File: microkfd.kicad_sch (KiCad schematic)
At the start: 47 parts, among them J1 USB_B_Micro, J2 AudioJack3, J3 OLED, Q1 2N7002, Q2 2N7002, SW1 RST, SW2 DOWN, SW3 ENT, SW4 UP, U1 SP3003-02, U2 ATmega32U4RC-A, Y1 16MHz

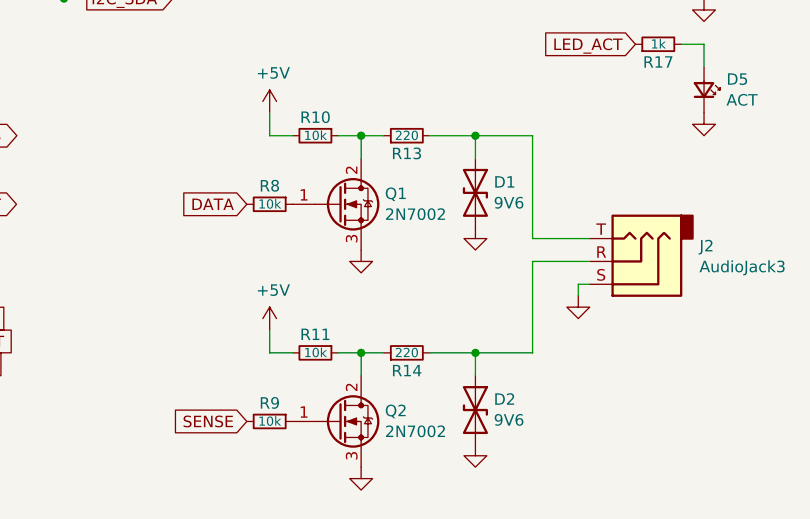
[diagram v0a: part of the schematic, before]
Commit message: finalized rev B
switched MOSFETs due to parts availability, regenerated gerbers
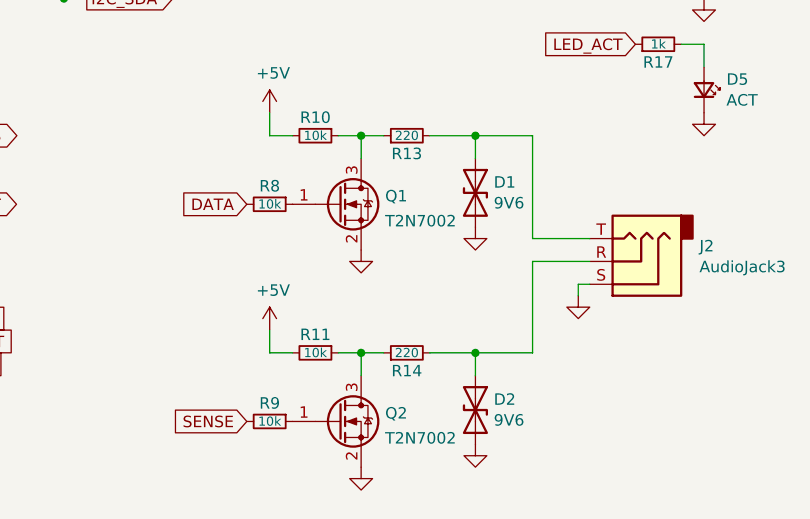
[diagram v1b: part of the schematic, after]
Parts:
- removed Q1, Q2: 2N7002, Package_TO_SOT_SMD:SOT-23_Handsoldering, symbol Device:Q_NMOS_GDS
- added Q1, Q2: T2N7002, Package_TO_SOT_SMD:SOT-23_Handsoldering, symbol Device:Q_NMOS_GSD
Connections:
- net GND: now also Q1.2 (S), Q2.2 (S)
- net at R8.1: now also Q1.1 (G)
- net at R10.1, R13.1: now also Q1.3 (D)
- net at R9.1: now also Q2.1 (G)
- net at R11.1, R14.1: now also Q2.3 (D)
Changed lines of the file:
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@@
     (pin "1")
-  )
-  (symbol (lib_id "Device:Q_NMOS_GDS") (at 162.56 114.3 0) (unit 1)
-    (in_bom yes) (on_board yes)
-    (property "Reference" "Q1" (id 0) (at 167.7416 113.1316 0)
-      (effects (font (size 1.27 1.27)) (justify left))
-    )
-    (property "Value" "2N7002" (id 1) (at 167.7416 115.443 0)
-      (effects (font (size 1.27 1.27)) (justify left))
-    )
-    (property "Footprint" "Package_TO_SOT_SMD:SOT-23_Handsoldering" (id 2) (at 167.64 111.76 0)
-      (effects (font (size 1.27 1.27)) hide)
-    )
-    (property "Datasheet" "~" (id 3) (at 162.56 114.3 0)
-      (effects (font (size 1.27 1.27)) hide)
-    )
-    (pin "1")
-    (pin "2")
-    (pin "3")
   )
   (symbol (lib_id "Device:R_Small") (at 154.94 114.3 270) (unit 1)
@@
     (pin "1")
   )
-  (symbol (lib_id "Device:Q_NMOS_GDS") (at 162.56 138.43 0) (unit 1)
-    (in_bom yes) (on_board yes)
-    (property "Reference" "Q2" (id 0) (at 167.7416 137.2616 0)
-      (effects (font (size 1.27 1.27)) (justify left))
-    )
-    (property "Value" "2N7002" (id 1) (at 167.7416 139.573 0)
-      (effects (font (size 1.27 1.27)) (justify left))
-    )
-    (property "Footprint" "Package_TO_SOT_SMD:SOT-23_Handsoldering" (id 2) (at 167.64 135.89 0)
-      (effects (font (size 1.27 1.27)) hide)
-    )
-    (property "Datasheet" "~" (id 3) (at 162.56 138.43 0)
-      (effects (font (size 1.27 1.27)) hide)
-    )
-    (pin "1")
-    (pin "2")
-    (pin "3")
-  )
   (symbol (lib_id "Device:R_Small") (at 154.94 138.43 270) (unit 1)
     (in_bom yes) (on_board yes)
@@
     (pin "1")
     (pin "2")
+  )
+  (symbol (lib_id "Device:Q_NMOS_GSD") (at 162.56 114.3 0) (unit 1)
+    (in_bom yes) (on_board yes) (fields_autoplaced)
+    (property "Reference" "Q1" (id 0) (at 167.767 113.3915 0)
+      (effects (font (size 1.27 1.27)) (justify left))
+    )
+    (property "Value" "T2N7002" (id 1) (at 167.767 116.1666 0)
+      (effects (font (size 1.27 1.27)) (justify left))
+    )
+    (property "Footprint" "Package_TO_SOT_SMD:SOT-23_Handsoldering" (id 2) (at 167.64 111.76 0)
+      (effects (font (size 1.27 1.27)) hide)
+    )
+    (property "Datasheet" "~" (id 3) (at 162.56 114.3 0)
+      (effects (font (size 1.27 1.27)) hide)
+    )
+    (pin "1")
+    (pin "2")
+    (pin "3")
   )
   (symbol (lib_id "MCU_Microchip_ATmega:ATmega32U4RC-A") (at 101.6 96.52 0) (unit 1)
@@
     (pin "9")
   )
+  (symbol (lib_id "Device:Q_NMOS_GSD") (at 162.56 138.43 0) (unit 1)
+    (in_bom yes) (on_board yes) (fields_autoplaced)
+    (property "Reference" "Q2" (id 0) (at 167.767 137.5215 0)
+      (effects (font (size 1.27 1.27)) (justify left))
+    )
+    (property "Value" "T2N7002" (id 1) (at 167.767 140.2966 0)
+      (effects (font (size 1.27 1.27)) (justify left))
+    )
+    (property "Footprint" "Package_TO_SOT_SMD:SOT-23_Handsoldering" (id 2) (at 167.64 135.89 0)
+      (effects (font (size 1.27 1.27)) hide)
+    )
+    (property "Datasheet" "~" (id 3) (at 162.56 138.43 0)
+      (effects (font (size 1.27 1.27)) hide)
+    )
+    (pin "1")
+    (pin "2")
+    (pin "3")
+  )
   (sheet_instances
     (path "/" (page "1"))
@@
       (reference "J3") (unit 1) (value "OLED") (footprint "Connector_PinSocket_2.54mm:PinSocket_1x04_P2.54mm_Vertical_SMD_Pin1Left")
     )
-    (path "/00000000-0000-0000-0000-000061af1fd1"
-      (reference "Q1") (unit 1) (value "2N7002") (footprint "Package_TO_SOT_SMD:SOT-23_Handsoldering")
-    )
-    (path "/00000000-0000-0000-0000-000061ba989c"
-      (reference "Q2") (unit 1) (value "2N7002") (footprint "Package_TO_SOT_SMD:SOT-23_Handsoldering")
+    (path "/5f7c53ad-a221-4a7c-aa56-8fe23dde6e72"
+      (reference "Q1") (unit 1) (value "T2N7002") (footprint "Package_TO_SOT_SMD:SOT-23_Handsoldering")
+    )
+    (path "/a8941a1d-02e4-4d2e-8a0e-8e48b9dc4893"
+      (reference "Q2") (unit 1) (value "T2N7002") (footprint "Package_TO_SOT_SMD:SOT-23_Handsoldering")
     )
     (path "/00000000-0000-0000-0000-000061ae9c86"

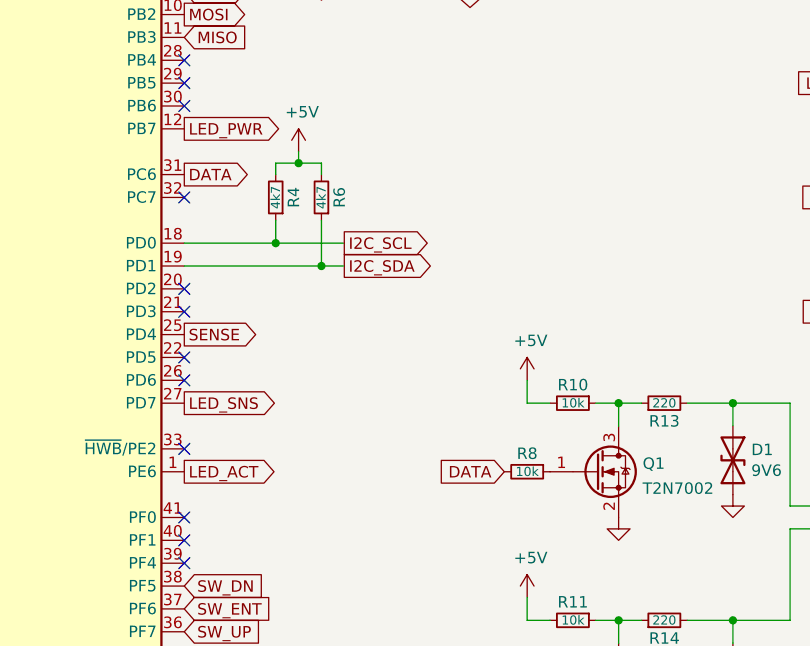
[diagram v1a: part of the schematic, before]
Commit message: revC updates
fixed missing data input line (now runs to PC2 interrupt pin)
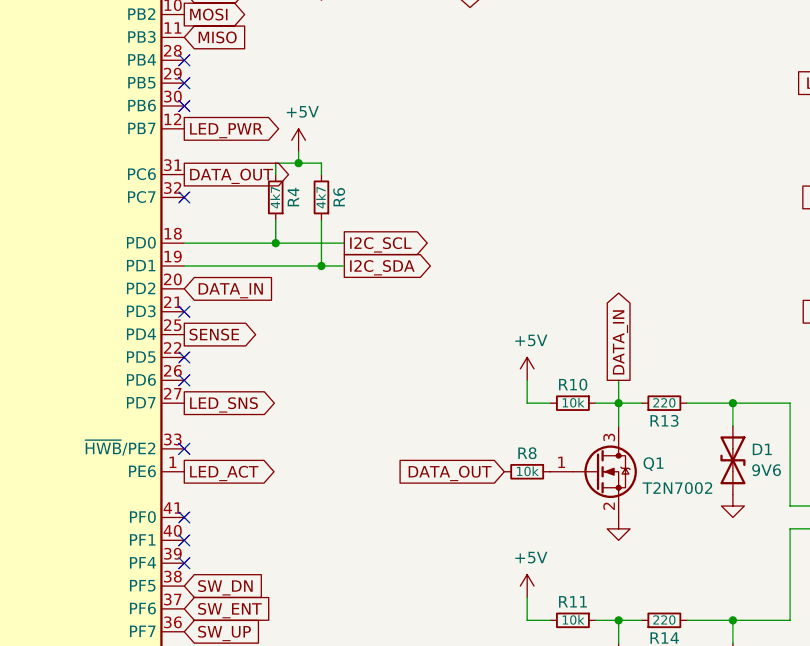
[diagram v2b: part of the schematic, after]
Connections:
- net DATA_IN: now reaches Q1.3 (D), R10.1, R13.1
- net DATA_IN: now also U2.20 (PD2)
- net DATA renamed DATA_OUT
- no-connect marks 15 -> 14
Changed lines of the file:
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@@
   (title_block
     (title "MicroKFD")
-    (date "2021-12-06")
-    (rev "A")
+    (date "2022-01-19")
+    (rev "C")
     (company "W3AXL")
-    (comment 2 "https://github.com/jelimoore/KFDtool")
-    (comment 3 "Based on the KFDShield")
+    (comment 1 "https://github.com/jelimoore/KFDtool")
+    (comment 2 "Based on the KFDShield")
+    (comment 4 "2022-01-19: Fixed missing data input line")
   )
   (junction (at 127 88.9) (diameter 0) (color 0 0 0 0)
@@
   (junction (at 76.2 78.74) (diameter 0) (color 0 0 0 0)
   )
-  (no_connect (at 116.84 93.98))
   (no_connect (at 116.84 96.52))
   (no_connect (at 116.84 58.42))
@@
     (stroke (width 0) (type default) (color 0 0 0 0))
   )
+  (wire (pts (xy 165.1 104.14) (xy 165.1 106.68))
+    (stroke (width 0) (type default) (color 0 0 0 0))
+  )
   (wire (pts (xy 195.58 55.88) (xy 195.58 48.26))
     (stroke (width 0) (type default) (color 0 0 0 0))
@@
     (effects (font (size 1.27 1.27)) (justify left bottom))
   )
-  (global_label "DATA" (shape output) (at 116.84 81.28 0) (fields_autoplaced)
-    (effects (font (size 1.27 1.27)) (justify left))
-    (property "Intersheet References" "${INTERSHEET_REFS}" (id 0) (at 0 0 0)
-      (effects (font (size 1.27 1.27)) hide)
+  (global_label "DATA_IN" (shape input) (at 116.84 93.98 0) (fields_autoplaced)
+    (effects (font (size 1.27 1.27)) (justify left))
+    (property "Intersheet References" "${INTERSHEET_REFS}" (id 0) (at 126.4818 93.9006 0)
+      (effects (font (size 1.27 1.27)) (justify left) hide)
+    )
+  )
+  (global_label "DATA_OUT" (shape output) (at 116.84 81.28 0) (fields_autoplaced)
+    (effects (font (size 1.27 1.27)) (justify left))
+    (property "Intersheet References" "${INTERSHEET_REFS}" (id 0) (at 128.1752 81.2006 0)
+      (effects (font (size 1.27 1.27)) (justify left) hide)
     )
   )
@@
     )
   )
-  (global_label "DATA" (shape input) (at 152.4 114.3 180) (fields_autoplaced)
+  (global_label "DATA_OUT" (shape input) (at 152.4 114.3 180) (fields_autoplaced)
     (effects (font (size 1.27 1.27)) (justify right))
-    (property "Intersheet References" "${INTERSHEET_REFS}" (id 0) (at 0 0 0)
-      (effects (font (size 1.27 1.27)) hide)
+    (property "Intersheet References" "${INTERSHEET_REFS}" (id 0) (at 141.0648 114.2206 0)
+      (effects (font (size 1.27 1.27)) (justify right) hide)
     )
   )
@@
     )
   )
+  (global_label "DATA_IN" (shape output) (at 165.1 104.14 90) (fields_autoplaced)
+    (effects (font (size 1.27 1.27)) (justify left))
+    (property "Intersheet References" "${INTERSHEET_REFS}" (id 0) (at 165.0206 94.4982 90)
+      (effects (font (size 1.27 1.27)) (justify left) hide)
+    )
+  )

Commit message: rev D: fixed pin mappings
changed pin mappings to be closer to original KFDShield, added correct sense and data lines
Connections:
- net SW_DN: now also U2.37 (PF6); no longer U2.38 (PF5)
- net SW_ENT: now also U2.38 (PF5); no longer U2.37 (PF6)
- net SENSE_IN: now reaches Q2.3 (D), R11.1, R14.1
- net SENSE_IN: now also U2.21 (PD3)
- net SENSE renamed SENSE_OUT
- no-connect marks 14 -> 13
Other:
- moved on the sheet: R4, R6

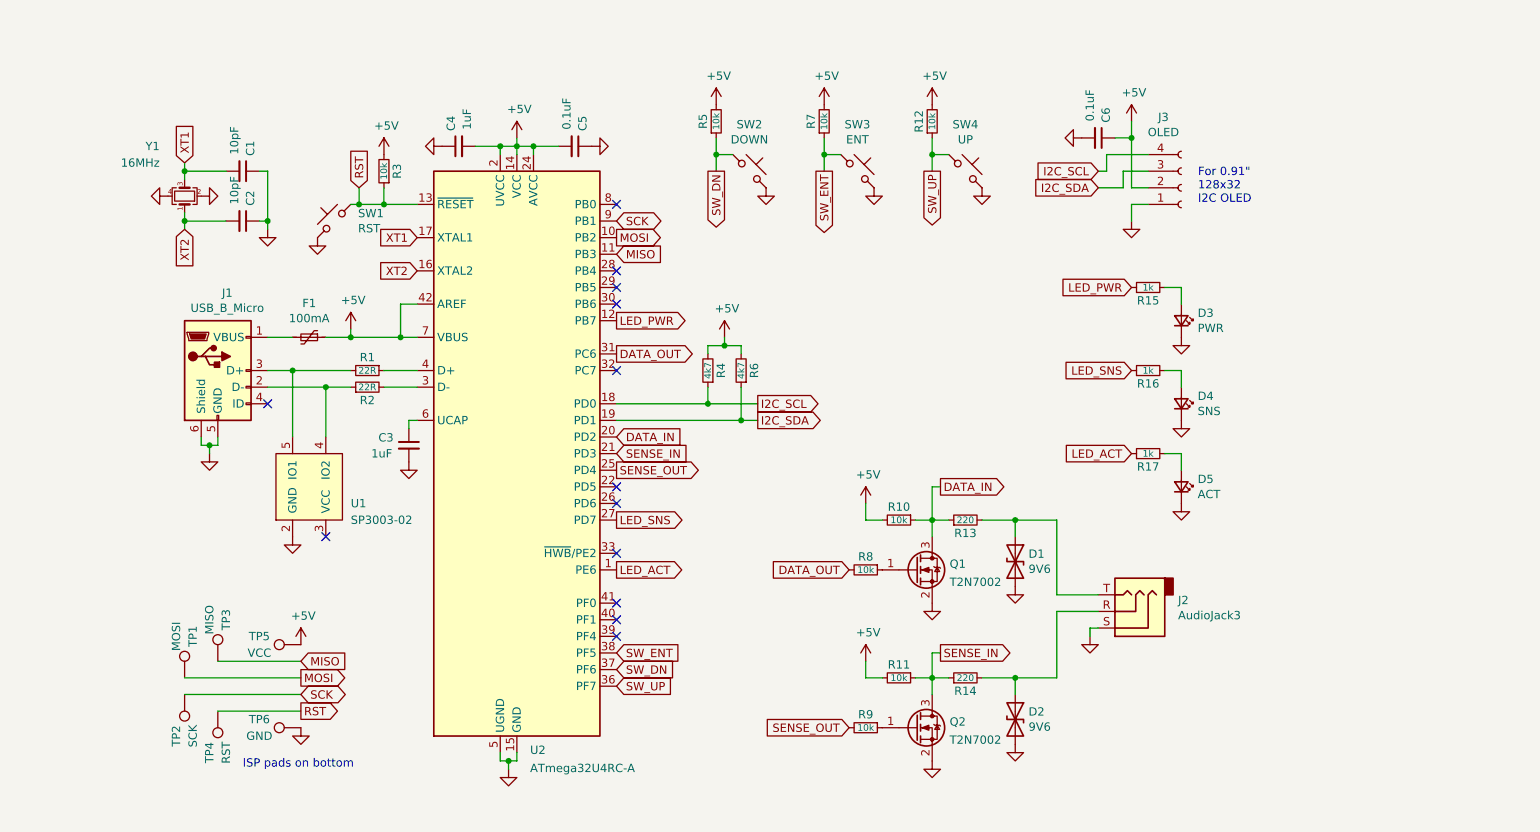
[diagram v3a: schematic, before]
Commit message: revision E - atmega328p redesign
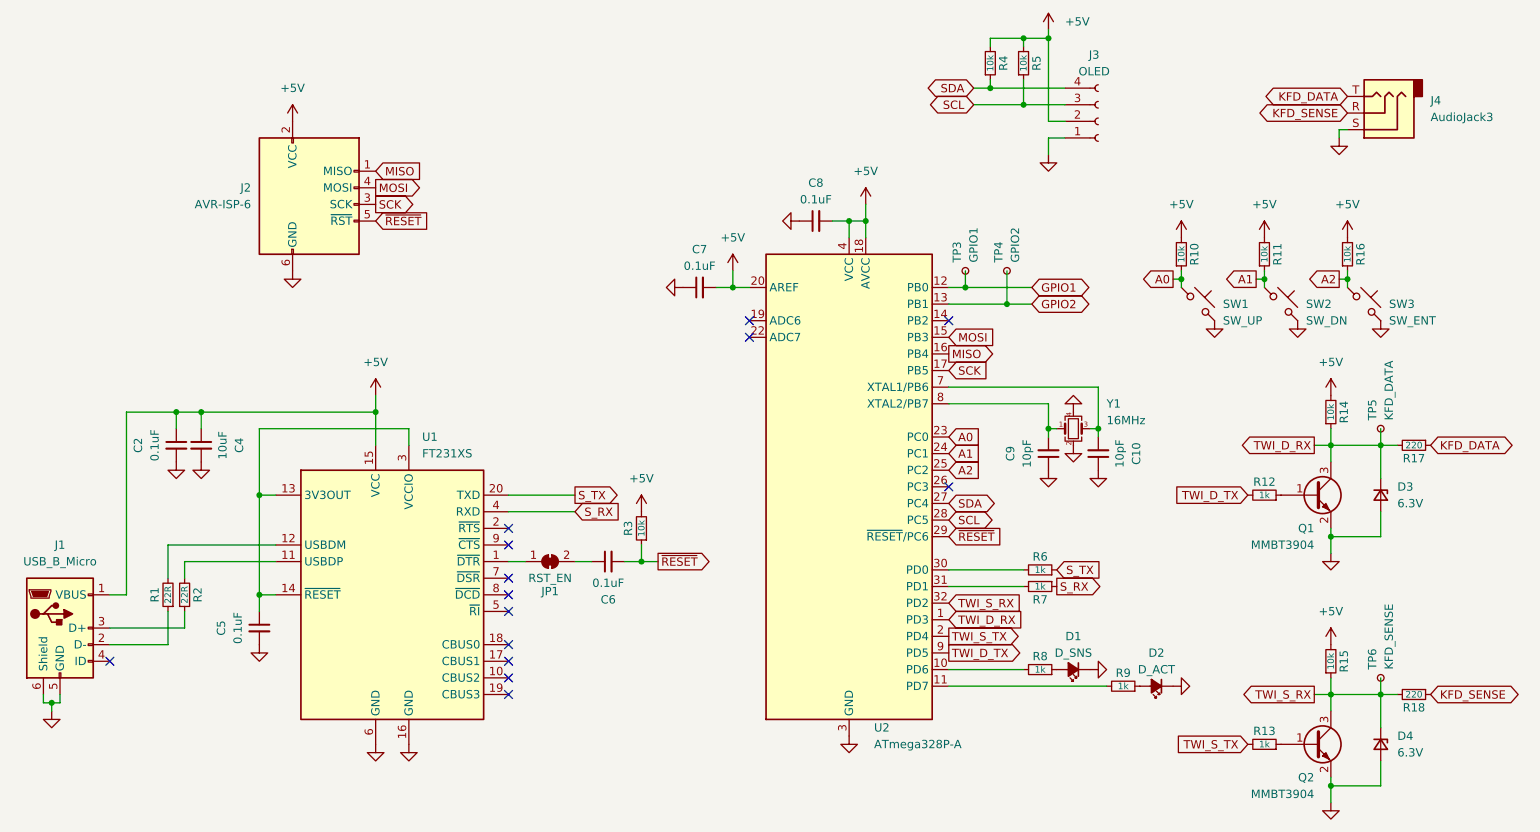
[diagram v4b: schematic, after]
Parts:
- removed C1: 10pF, Capacitor_SMD:C_0805_2012Metric_Pad1.18x1.45mm_HandSolder, symbol Device:C_Small
- removed C3: 1uF, Capacitor_SMD:C_0805_2012Metric_Pad1.18x1.45mm_HandSolder, symbol Device:C_Small
- removed D1, D2: 9V6, Diode_SMD:D_0805_2012Metric_Pad1.15x1.40mm_HandSolder, symbol Device:D_TVS
- removed D3: PWR, Diode_SMD:D_0805_2012Metric_Pad1.15x1.40mm_HandSolder, symbol Device:LED_Small
- removed D4: SNS, Diode_SMD:D_0805_2012Metric_Pad1.15x1.40mm_HandSolder, symbol Device:LED_Small
- removed D5: ACT, Diode_SMD:D_0805_2012Metric_Pad1.15x1.40mm_HandSolder, symbol Device:LED_Small
- removed F1: 100mA, Fuse:Fuse_0805_2012Metric_Pad1.15x1.40mm_HandSolder, symbol Device:Polyfuse_Small
- removed J2: AudioJack3, Connector_Audio:Jack_3.5mm_CUI_SJ-3523-SMT_Horizontal, symbol Connector:AudioJack3
- removed Q1, Q2: T2N7002, Package_TO_SOT_SMD:SOT-23_Handsoldering, symbol Device:Q_NMOS_GSD
- removed SW4: UP, Button_Switch_SMD:Panasonic_EVQPUM_EVQPUD, symbol Switch:SW_Push_45deg
- removed TP1: MOSI, TestPoint:TestPoint_Pad_1.0x1.0mm, symbol Connector:TestPoint
- removed TP2: SCK, TestPoint:TestPoint_Pad_1.0x1.0mm, symbol Connector:TestPoint
- removed TP3: MISO, TestPoint:TestPoint_Pad_1.0x1.0mm, symbol Connector:TestPoint
- removed TP4: RST, TestPoint:TestPoint_Pad_1.0x1.0mm, symbol Connector:TestPoint
- removed TP5: VCC, TestPoint:TestPoint_Pad_1.0x1.0mm, symbol Connector:TestPoint
- removed TP6: GND, TestPoint:TestPoint_Pad_1.0x1.0mm, symbol Connector:TestPoint
- removed U1: SP3003-02, Package_TO_SOT_SMD:SOT-553, symbol sp3003:SP3003-02
- removed U2: ATmega32U4RC-A, Package_QFP:TQFP-44_10x10mm_P0.8mm, symbol MCU_Microchip_ATmega:ATmega32U4RC-A
- added C10, C9: 10pF, Capacitor_SMD:C_0603_1608Metric_Pad1.08x0.95mm_HandSolder, symbol Device:C_Small
- added C7, C8: 0.1uF, Capacitor_SMD:C_0603_1608Metric_Pad1.08x0.95mm_HandSolder, symbol Device:C_Small
- added D1: D_SNS, LED_SMD:LED_0603_1608Metric_Pad1.05x0.95mm_HandSolder, symbol Device:LED_Small_Filled
- added D2: D_ACT, LED_SMD:LED_0603_1608Metric_Pad1.05x0.95mm_HandSolder, symbol Device:LED_Small_Filled
- added D3, D4: 6.3V, Diode_SMD:D_SOD-323_HandSoldering, symbol Device:D_Zener_Small
- added J2: AVR-ISP-6, Connector_PinHeader_2.54mm:PinHeader_2x03_P2.54mm_Vertical_SMD, symbol Connector:AVR-ISP-6
- added J4: AudioJack3, Connector_Audio:Jack_3.5mm_CUI_SJ-3523-SMT_Horizontal, symbol Connector:AudioJack3
- added JP1: RST_EN, Jumper:SolderJumper-2_P1.3mm_Bridged_RoundedPad1.0x1.5mm, symbol Jumper:SolderJumper_2_Bridged
- added Q1, Q2: MMBT3904, Package_TO_SOT_SMD:SOT-23, symbol Transistor_BJT:MMBT3904
- added R18: 220, Resistor_SMD:R_0603_1608Metric_Pad0.98x0.95mm_HandSolder, symbol Device:R_Small
- added TP3: GPIO1, TestPoint:TestPoint_Pad_1.0x1.0mm, symbol Connector:TestPoint_Small
- added TP4: GPIO2, TestPoint:TestPoint_Pad_1.0x1.0mm, symbol Connector:TestPoint_Small
- added TP5: KFD_DATA, TestPoint:TestPoint_Pad_1.0x1.0mm, symbol Connector:TestPoint_Small
- added TP6: KFD_SENSE, TestPoint:TestPoint_Pad_1.0x1.0mm, symbol Connector:TestPoint_Small
- added U1: FT231XS, Package_SO:SSOP-20_3.9x8.7mm_P0.635mm, symbol Interface_USB:FT231XS
- added U2: ATmega328P-A, Package_QFP:TQFP-32_7x7mm_P0.8mm, symbol MCU_Microchip_ATmega:ATmega328P-A
- C2: value 10pF -> 0.1uF; footprint Capacitor_SMD:C_0805_2012Metric_Pad1.18x1.45mm_HandSolder -> Capacitor_SMD:C_0603_1608Metric_Pad1.08x0.95mm_HandSolder
- C4: value 1uF -> 10uF; footprint Capacitor_SMD:C_0805_2012Metric_Pad1.18x1.45mm_HandSolder -> Capacitor_SMD:C_0603_1608Metric_Pad1.08x0.95mm_HandSolder
- C5, C6: footprint Capacitor_SMD:C_0805_2012Metric_Pad1.18x1.45mm_HandSolder -> Capacitor_SMD:C_0603_1608Metric_Pad1.08x0.95mm_HandSolder
- J1: footprint Connector_USB:USB_Micro-B_Wuerth_629105150521_CircularHoles -> Connector_USB:USB_Micro-B_Wuerth_629105150521
- J3: footprint Connector_PinSocket_2.54mm:PinSocket_1x04_P2.54mm_Vertical_SMD_Pin1Left -> Connector_PinHeader_2.54mm:PinHeader_1x04_P2.54mm_Vertical_SMD_Pin1Right
- R1, R10, R11, R2, R3, R5: footprint Resistor_SMD:R_0805_2012Metric_Pad1.20x1.40mm_HandSolder -> Resistor_SMD:R_0603_1608Metric_Pad0.98x0.95mm_HandSolder
- R12, R7, R8, R9: value 10k -> 1k; footprint Resistor_SMD:R_0805_2012Metric_Pad1.20x1.40mm_HandSolder -> Resistor_SMD:R_0603_1608Metric_Pad0.98x0.95mm_HandSolder
- R13: value 220 -> 1k; footprint Resistor_SMD:R_0805_2012Metric_Pad1.20x1.40mm_HandSolder -> Resistor_SMD:R_0603_1608Metric_Pad0.98x0.95mm_HandSolder
- R14: value 220 -> 10k; footprint Resistor_SMD:R_0805_2012Metric_Pad1.20x1.40mm_HandSolder -> Resistor_SMD:R_0603_1608Metric_Pad0.98x0.95mm_HandSolder
- R15, R16: value 1k -> 10k; footprint Resistor_SMD:R_0805_2012Metric_Pad1.20x1.40mm_HandSolder -> Resistor_SMD:R_0603_1608Metric_Pad0.98x0.95mm_HandSolder
- R17: value 1k -> 220; footprint Resistor_SMD:R_0805_2012Metric_Pad1.20x1.40mm_HandSolder -> Resistor_SMD:R_0603_1608Metric_Pad0.98x0.95mm_HandSolder
- R4: value 4k7 -> 10k; footprint Resistor_SMD:R_0805_2012Metric_Pad1.20x1.40mm_HandSolder -> Resistor_SMD:R_0603_1608Metric_Pad0.98x0.95mm_HandSolder
- R6: value 4k7 -> 1k; footprint Resistor_SMD:R_0805_2012Metric_Pad1.20x1.40mm_HandSolder -> Resistor_SMD:R_0603_1608Metric_Pad0.98x0.95mm_HandSolder
- SW1: value RST -> SW_UP; footprint Button_Switch_SMD:SW_Push_1P1T_NO_CK_KMR2 -> Button_Switch_SMD:Panasonic_EVQPUM_EVQPUD
- SW2: value DOWN -> SW_DN
- SW3: value ENT -> SW_ENT
- Y1: footprint Crystal:Crystal_SMD_SeikoEpson_FA238-4Pin_3.2x2.5mm_HandSoldering -> Crystal:Crystal_SMD_SeikoEpson_FA238V-4Pin_3.2x2.5mm_HandSoldering
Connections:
- net +5V: now also C2.1, C4.1, J1.1 (VBUS), R14.2, R15.2, R16.2, C7.2, C8.2, J2.2 (VCC), U1.15 (VCC), U2.18 (AVCC), U2.20 (AREF), U2.4 (VCC), U2.6 (VCC); no longer C4.2, C5.2, C6.1, R12.2, R6.2, R7.2
- net GND: now also C2.2, C4.2, C5.2, SW1.2, C10.1, C7.1, C8.1, C9.1, D1.1 (K), D2.1 (K), D3.2 (A), D4.2 (A), J2.6 (GND), J4.S, Q1.2 (E), Q2.2 (E), U1.16 (GND), U1.6 (GND), U2.21 (GND), U2.3 (GND), U2.5 (GND); no longer C2.1, C4.1, C5.1, C6.2, SW1.1
- net MISO: now also J2.1 (MISO), U2.16 (PB4)
- net MOSI: now also J2.4 (MOSI), U2.15 (PB3)
- net SCK: now also J2.3 (SCK), U2.17 (PB5)
- net at R2.1: now also J1.3 (D+); no longer J1.2 (D-)
- net at R1.2: now also U1.12 (USBDM); no longer J1.3 (D+)
- net at R1.1: now also J1.2 (D-)
- net at R2.2: now also U1.11 (USBDP)
- net at R8.1: now also D1.2 (A)
- net TWI_S_TX: now reaches R13.2
- net TWI_S_TX: now also U2.2 (PD4)
- net at R9.1: now also D2.2 (A)
- net TWI_D_RX: now reaches R17.2
- net TWI_D_RX: now also R14.1, D3.1 (K), Q1.3 (C), TP5.1, U2.1 (PD3)
- net DATA_IN: no longer names the net of R13.1
- net DATA_IN: now also Q2.1 (B); no longer R10.1
- net DATA_OUT: no longer names the net of R8.2
- net DATA_OUT: now also U2.10 (PD6)
- net I2C_SCL renamed SDA
- net SDA: now also U2.27 (PC4)
- net I2C_SDA renamed SCL
- net SCL: now also R5.1, U2.28 (PC5); no longer R6.1
- net LED_ACT renamed KFD_DATA
- net KFD_DATA: now also J4.T
- net LED_PWR renamed TWI_S_RX
- net TWI_S_RX: now also D4.1 (K), Q2.3 (C), R18.2, TP6.1, U2.32 (PD2)
- net LED_SNS renamed A2
- net A2: now also SW3.1, U2.25 (PC2)
- net RST renamed ~{RESET}
- net ~{RESET}: now also C6.2, J2.5 (~{RST}), U2.29 (~{RESET}/PC6); no longer SW1.2
- net SENSE_IN renamed A1
- net A1: now also SW2.1, U2.24 (PC1); no longer R14.1
- net SENSE_OUT: no longer names the net of R9.2
- net SENSE_OUT: now also U2.11 (PD7)
- removed net SW_DN: R5.1, SW2.1
- net SW_ENT renamed S_RX
- net S_RX: now also U1.4 (RXD); no longer SW3.1
- net SW_UP: no longer names the net of R12.1
- net SW_UP: now also Q1.1 (B)
- net XT1: no longer names the net of Y1.3
- net XT1: now also C10.2, U2.7 (XTAL1/PB6)
- net XT2: no longer names the net of Y1.1
- net XT2: now also C9.2, U2.8 (XTAL2/PB7); no longer C2.2
- new net: JP1.1 (A), U1.1 (~{DTR})
- new net: C5.1, U1.13 (3V3OUT), U1.14 (~{RESET}), U1.3 (VCCIO)
- new net: R6.2, U2.30 (PD0)
- new net: R7.2, U2.31 (PD1)
- new net: C6.1, JP1.2 (B)
- new net A0: R10.1, SW1.1, U2.23 (PC0)
- new net GPIO1: TP3.1, U2.12 (PB0)
- new net GPIO2: TP4.1, U2.13 (PB1)
- new net KFD_SENSE: J4.R, R18.1
- new net S_TX: R6.1, U1.20 (TXD)
- new net TWI_D_TX: R12.2, U2.9 (PD5)
- no-connect marks 13 -> 14
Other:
- note removed: "For 0.91" 128x32 I2C OLED"
- note removed: "ISP pads on bottom"
